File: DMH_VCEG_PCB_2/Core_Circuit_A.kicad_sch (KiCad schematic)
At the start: 78 parts, among them J22 Conn_01x10_PinHeader, Q1 BC548, Q2 BC558, Q3 BC548, SW1 SW_DPDT_x2, U1 TL074, U2 4001, U3 40106, U4 CD4066BE, U5 TL074, U6 TL074, U7 TL074

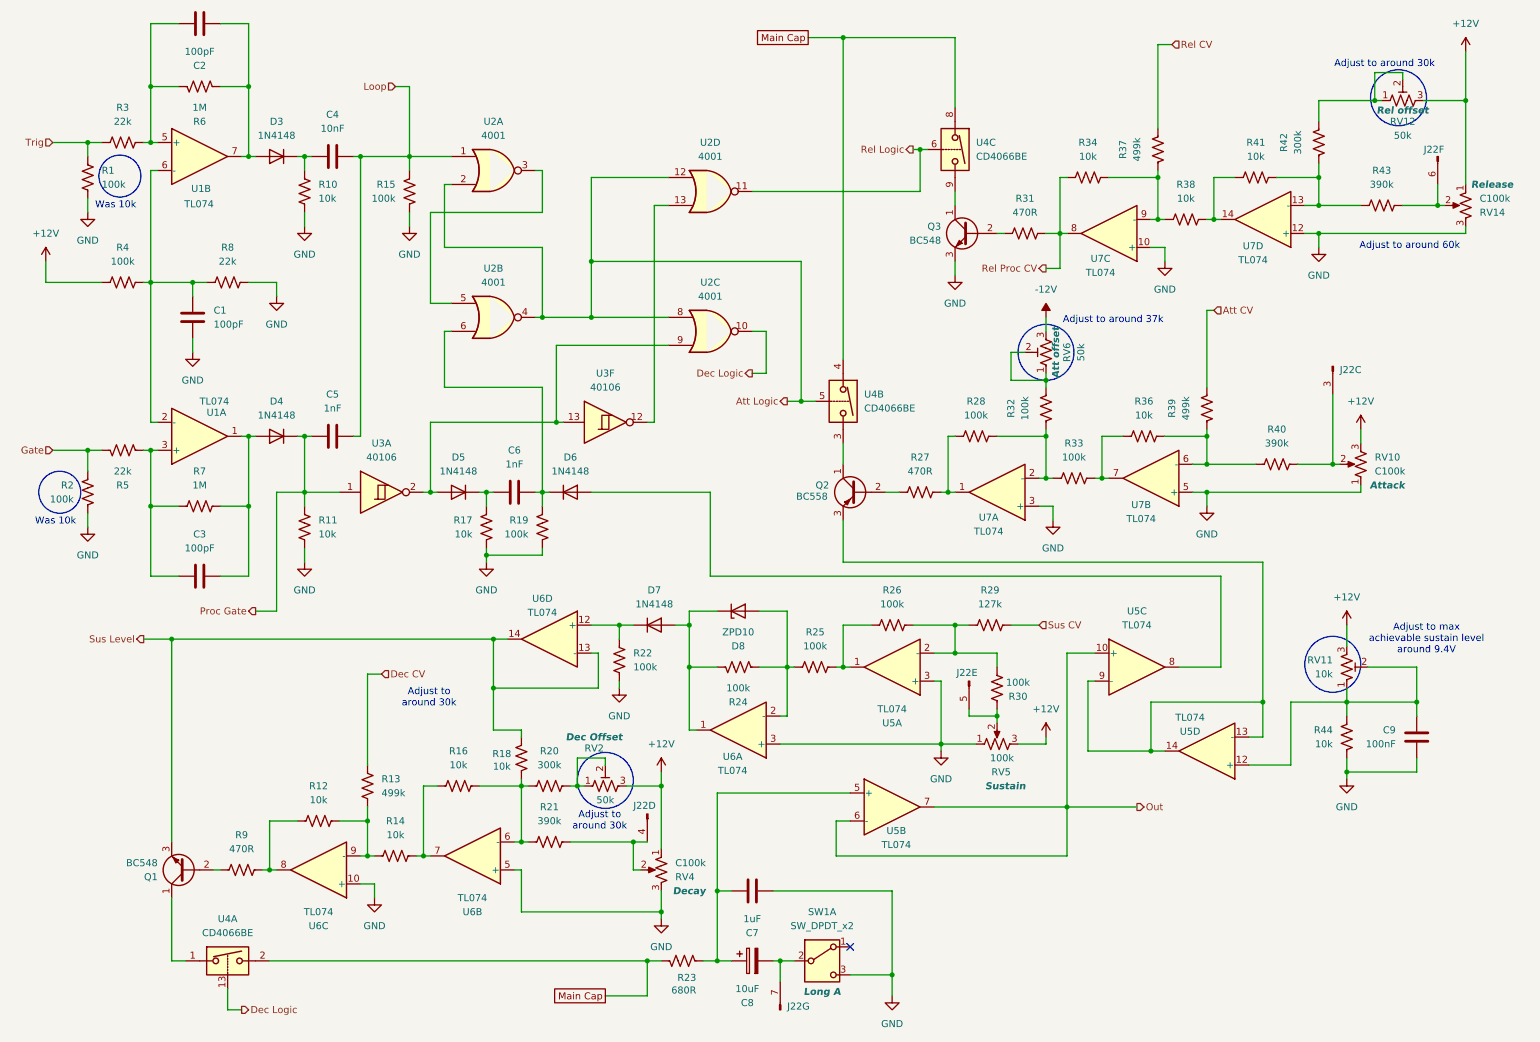
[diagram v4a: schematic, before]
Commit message: Synced PCB 2 project with PCB 1
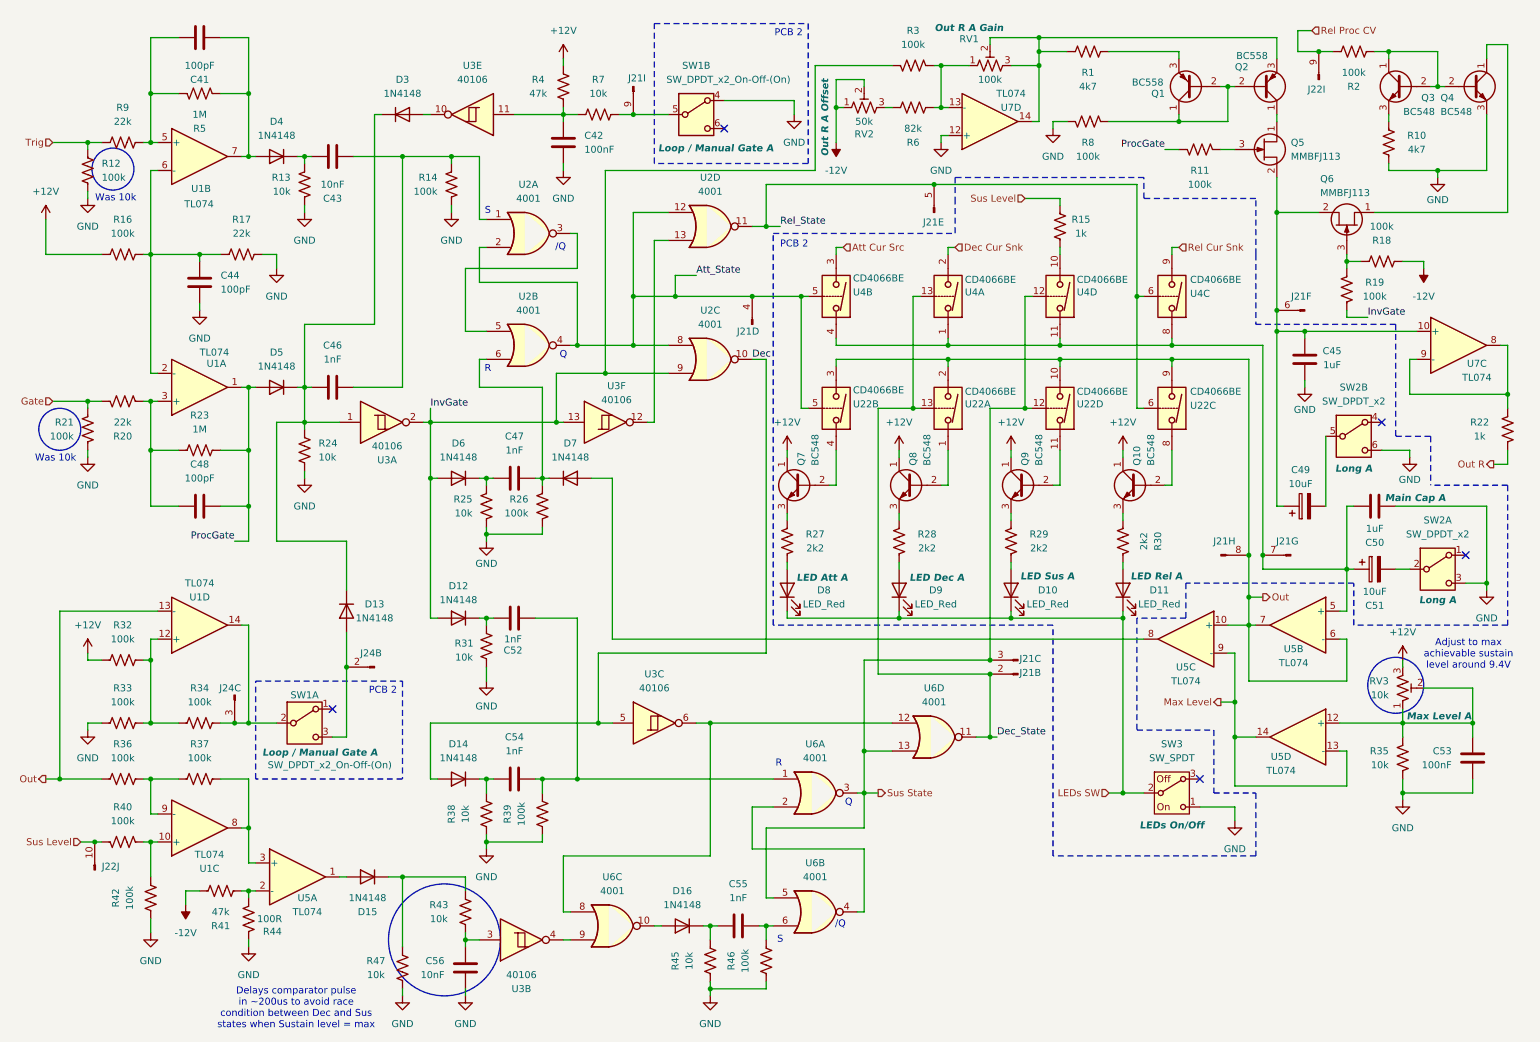
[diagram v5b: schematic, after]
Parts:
- removed D7: 1N4148, Diode_THT:D_DO-35_SOD27_P7.62mm_Horizontal, symbol Diode:1N4148
- removed D8: ZPD10, Diode_THT:D_DO-35_SOD27_P7.62mm_Horizontal, symbol Diode:ZPDxx
- removed J22: Conn_01x10_PinHeader, Connector_PinSocket_2.54mm:PinSocket_1x10_P2.54mm_Vertical, symbol SynthStuff:Conn_01x10_PinHeader
- removed Q1: BC548, Package_TO_SOT_THT:TO-92L_Inline_Wide, symbol Transistor_BJT:BC548
- removed R12, R14, R16: 10k, Resistor_THT:R_Axial_DIN0207_L6.3mm_D2.5mm_P7.62mm_Horizontal, symbol Device:R_US
- removed R13: 499k, Resistor_THT:R_Axial_DIN0207_L6.3mm_D2.5mm_P7.62mm_Horizontal, symbol Device:R_US
- removed R20: 300k, Resistor_THT:R_Axial_DIN0207_L6.3mm_D2.5mm_P7.62mm_Horizontal, symbol Device:R_US
- removed R21: 390k, Resistor_THT:R_Axial_DIN0207_L6.3mm_D2.5mm_P7.62mm_Horizontal, symbol Device:R_US
- removed R23: 680R, Resistor_THT:R_Axial_DIN0207_L6.3mm_D2.5mm_P7.62mm_Horizontal, symbol Device:R_US
- removed R24, R25, R26: 100k, Resistor_THT:R_Axial_DIN0207_L6.3mm_D2.5mm_P7.62mm_Horizontal, symbol Device:R_US
- removed R9: 470R, Resistor_THT:R_Axial_DIN0207_L6.3mm_D2.5mm_P7.62mm_Horizontal, symbol Device:R_US
- removed RV10, RV14, RV4: C100k, SynthStuff:Potentiometer_Alpha_RD901F-40-00D_Single_Vertical, symbol Device:R_Potentiometer_US
- removed RV12, RV6: 50k, Potentiometer_THT:Potentiometer_Bourns_3296W_Vertical, symbol Device:R_Potentiometer_Trim_US
- removed RV5: 100k, SynthStuff:Potentiometer_Alpha_RD901F-40-00D_Single_Vertical, symbol Device:R_Potentiometer_US
- removed U6: TL074, Package_DIP:DIP-14_W7.62mm_Socket, symbol Amplifier_Operational:TL074
- removed unit 2 of U7
- removed unit 1 of U7
- added C42: 100nF, Capacitor_THT:C_Disc_D4.3mm_W1.9mm_P5.00mm, symbol Device:C
- added C45: 1uF, Capacitor_THT:C_Rect_L7.0mm_W4.5mm_P5.00mm, symbol Device:C
- added C49: 10uF, Capacitor_THT:CP_Radial_D4.0mm_P1.50mm, symbol Device:C_Polarized
- added C52, C54, C55: 1nF, Capacitor_THT:C_Disc_D4.3mm_W1.9mm_P5.00mm, symbol Device:C
- added C56: 10nF, Capacitor_THT:C_Disc_D4.3mm_W1.9mm_P5.00mm, symbol Device:C
- added D10, D11, D8, D9: LED_Red, LED_THT:LED_D3.0mm, symbol Device:LED
- added D12, D13, D14, D15, D16, D3: 1N4148, Diode_THT:D_DO-35_SOD27_P7.62mm_Horizontal, symbol Diode:1N4148
- added J21: Conn_01x10_PinHeader, Connector_PinHeader_2.54mm:PinHeader_1x10_P2.54mm_Vertical, symbol SynthStuff:Conn_01x10_PinHeader
- added J22: Conn_01x10_PinHeader, Connector_PinSocket_2.54mm:PinSocket_1x10_P2.54mm_Vertical, symbol SynthStuff:Conn_01x10_PinHeader
- added J24: Conn_01x06_PinHeader, Connector_PinHeader_2.54mm:PinHeader_1x06_P2.54mm_Vertical, symbol SynthStuff:Conn_01x06_PinHeader
- added Q1: BC558, Package_TO_SOT_THT:TO-92L_Inline_Wide, symbol Transistor_BJT:BC558
- added Q10, Q4, Q7, Q8, Q9: BC548, Package_TO_SOT_THT:TO-92L_Inline_Wide, symbol Transistor_BJT:BC548
- added Q5, Q6: MMBFJ113, Package_TO_SOT_THT:TO-92L_Inline, symbol Transistor_FET:MMBFJ113
- added R1, R10: 4k7, Resistor_THT:R_Axial_DIN0207_L6.3mm_D2.5mm_P7.62mm_Horizontal, symbol Device:R_US
- added R11, R19, R2, R3, R46, R8: 100k, Resistor_THT:R_Axial_DIN0207_L6.3mm_D2.5mm_P7.62mm_Horizontal, symbol Device:R_US
- added R15: 1k, Resistor_THT:R_Axial_DIN0207_L6.3mm_D2.5mm_P7.62mm_Horizontal, symbol Device:R_US
- added R4: 47k, Resistor_THT:R_Axial_DIN0207_L6.3mm_D2.5mm_P7.62mm_Horizontal, symbol Device:R_US
- added R44: 100R, Resistor_THT:R_Axial_DIN0207_L6.3mm_D2.5mm_P7.62mm_Horizontal, symbol Device:R_US
- added R45, R47, R7: 10k, Resistor_THT:R_Axial_DIN0207_L6.3mm_D2.5mm_P7.62mm_Horizontal, symbol Device:R_US
- added R6: 82k, Resistor_THT:R_Axial_DIN0207_L6.3mm_D2.5mm_P7.62mm_Horizontal, symbol Device:R_US
- added RV1: 100k, Potentiometer_THT:Potentiometer_Bourns_3296W_Vertical, symbol Device:R_Potentiometer_Trim_US
- added SW1: SW_DPDT_x2_On-Off-(On), SynthStuff:Toggle_Switch_2_Poles_TE, symbol Switch:SW_DPDT_x2
- added unit 2 of SW2
- added SW3: SW_SPDT, SynthStuff:Toggle_Switch_TE, symbol SynthStuff:SW_SPDT_321_OnOff
- added unit 3 of U1
- added unit 4 of U1
- added U22: CD4066BE, Package_DIP:DIP-14_W7.62mm, symbol Analog_Switch:CD4066BE
- added unit 3 of U3
- added unit 2 of U3
- added unit 5 of U3
- added unit 4 of U4
- added U6: 4001, Package_DIP:DIP-14_W7.62mm_Socket, symbol 4xxx:4001
- C50: renamed from C7; footprint Capacitor_THT:C_Disc_D4.3mm_W1.9mm_P5.00mm -> Capacitor_THT:C_Rect_L7.0mm_W4.5mm_P5.00mm; Function (none) -> Main Cap A
- C51: renamed from C8; footprint Capacitor_THT:CP_Radial_D5.0mm_P2.00mm -> Capacitor_THT:CP_Radial_D4.0mm_P1.50mm
- R18, R34, R36: value 10k -> 100k
- R22: value 100k -> 1k
- R27: value 470R -> 2k2
- R28, R30: value 100k -> 2k2
- R29: value 127k -> 2k2
- R31: value 470R -> 10k
- R37, R39: value 499k -> 100k
- R40: value 390k -> 100k
- R41: value 10k -> 47k
- R42: value 300k -> 100k
- R43: value 390k -> 10k
- RV2: Function Dec Offset -> Out R A Offset
- RV3: renamed from RV11; Function (none) -> Max Level A
- renumbered C2 to C41, C4 to C43, C1 to C44, C5 to C46, C6 to C47, C3 to C48, C9 to C53, D3 to D4, D4 to D5, D5 to D6, D6 to D7, R1 to R12, R10 to R13, R15 to R14, R4 to R16, R8 to R17, R5 to R20, R2 to R21, R7 to R23, R11 to R24, R17 to R25, R19 to R26, R44 to R35, R6 to R5, R3 to R9, SW1 to SW2
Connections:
- net Att CV is gone; now on net GND: R39.2
- net +12V: now also R32.2, Q10.1 (C), Q7.1 (C), Q8.1 (C), Q9.1 (C), R4.1; no longer RV2.3
- net -12V: now also R18.1, R41.1, RV2.1, RV2.2
- net GND: now also R31.2, R33.2, R38.2, R42.2, C42.2, C45.1, C56.1, Q4.3 (E), R10.1, R44.2, R45.2, R46.2, R47.2, R8.2, SW1.4 (A), SW2.6 (C), SW3.1 (C); no longer Q3.3 (E), R22.1, U5.3 (+), U7.10 (+)
- net Out: now also R36.2, J21.8 (Pin_8), U1.13 (-), U22.10, U22.2, U22.3, U22.9
- net Rel Proc CV: now also J22.9 (Pin_9), R2.1; no longer R31.1, R34.2, U7.8
- net Sus Level: now also R40.1, J22.10 (Pin_10), R15.2; no longer R18.2
- net Max Level: now reaches U5.13 (-), U5.14, U5.9 (-)
- net Max Level: no longer Q2.3 (E)
- net at R22.2: now also U7.8, U7.9 (-)
- net at U5.1: now also D15.2 (A)
- net at R33.1: now also R32.1, R34.2, U1.12 (+); no longer R36.2
- net at C50.1, C51.1, U5.5 (+): now also U4.1, U4.4, U4.8, J21.7 (Pin_7), U4.11
- net at R43.1: now also D15.1 (K), R47.1
- net InvGate: now reaches D6.2 (A), U2.9, U3.13, U3.2
- net InvGate: now also D12.2 (A), R19.2, R3.1
- net at Q3.1 (C): now also Q3.2 (B), Q4.2 (B), R2.2; no longer U4.9
- net ProcGate: now reaches C48.2, D5.2 (A), R23.1, U1.1
- net ProcGate: now also R11.2
- net at Q2.1 (C): now also Q5.1 (D); no longer U4.3
- net at R27.2: now also D8.2 (A); no longer Q2.2 (B)
- net at R28.2: now also D9.2 (A); no longer R27.1
- net at R30.1: now also Q10.3 (E)
- net Att Logic renamed Att_State
- net Att_State: now also J21.4 (Pin_4), U22.5
- net Dec Logic renamed Dec
- net Dec: now also D14.2 (A), U3.5; no longer U4.13
- net Loop: no longer names the net of C43.2, C46.2, R14.2, U2.1
- removed net Main Cap: U4.2, U4.4, U4.8
- net Proc Gate: no longer names the net of C46.1, D5.1 (K), R24.2, U3.1
- net Proc Gate: now also D13.1 (K), D3.1 (K)
- net Rel CV: no longer names the net of R37.2
- net Rel CV: now also R36.1, U1.9 (-)
- net Rel Logic renamed Rel_State
- net Rel_State: now also J21.5 (Pin_5), U22.6
- net Sus CV: no longer names the net of R29.1
- net Sus CV: now also Q9.3 (E)
- new net: Q9.2 (B), U22.11
- new net: Q6.3 (G), R18.2, R19.1
- new net: C52.2, C54.2, R39.1, U6.1
- new net: C56.2, R43.2, U3.3
- new net: C45.2, C49.1, J21.6 (Pin_6), Q5.2 (S), Q6.2 (S), U7.10 (+)
- new net: J21.9 (Pin_9), R7.1, SW1.5 (B)
- new net: C42.1, R4.2, R7.2, U3.11
- new net: D16.2 (A), U6.10
- new net: U3.6, U6.12, U6.8
- new net: U3.4, U6.9
- new net: U6.2, U6.4
- new net: C55.2, R46.1, U6.6
- new net: C54.1, D14.1 (K), R38.1
- new net: Q5.3 (G), R11.1
- new net: R40.2, R42.1, U1.10 (+)
- new net: R37.1, U1.8, U5.3 (+)
- new net: R6.1, RV2.3
- new net: R3.2, R6.2, RV1.1, U7.13 (-)
- new net: Q10.2 (B), U22.8
- new net: Q7.3 (E), R27.1
- new net: Q2.3 (E), R1.1, RV1.2, RV1.3, U7.14
- new net: Q4.1 (C), Q6.1 (D)
- new net: Q1.1 (C), Q1.2 (B), Q2.2 (B), R8.1
- new net: Q1.3 (E), R1.2
- new net: D11.2 (A), R30.2
- new net: Q8.2 (B), U22.1
- new net: D3.2 (A), U3.10
- new net: C55.1, D16.1 (K), R45.1
- new net: C52.1, D12.1 (K), R31.1
- new net: Q7.2 (B), U22.4
- new net: R15.1, U4.10
- new net: R41.2, R44.1, U5.2 (-)
- new net: J24.3 (Pin_3), R34.1, SW1.2 (B), U1.14
- new net: D13.2 (A), J24.2 (Pin_2), SW1.3 (C)
- new net: Q8.3 (E), R28.1
- new net: C49.2, SW2.5 (B)
- new net: D10.2 (A), R29.2
- new net: Q3.3 (E), R10.2
- new net Att Cur Src: U4.3
- new net Dec Cur Snk: U4.2
- new net Dec_State: J21.2 (Pin_2), U22.13, U4.13, U6.11
- new net LEDs SW: D10.1 (K), D11.1 (K), D8.1 (K), D9.1 (K), SW3.2 (B)
- new net Out R: R22.1
- new net Rel Cur Snk: U4.9
- new net Sus State: J21.3 (Pin_3), U22.12, U4.12, U6.13, U6.3, U6.5
- no-connect marks 1 -> 5
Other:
- note added: "/Q"
- note added: "Delays comparator pulse in ~200us to avoid race condition between Dec and Sus states when Sustain level = max"
- note added: "PCB 2"
- note added: "Q"
- note added: "R"
- note added: "S"
- note removed: "Adjust to around 30k"
- note removed: "Adjust to around 37k"
- note removed: "Adjust to around 60k"
- moved on the sheet: C41, C44, C46, C47, C48, C50, C51, C53, D5, D6, D7, R12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

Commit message: Started placement on PCB 2
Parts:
- J21: footprint Connector_PinHeader_2.54mm:PinHeader_1x10_P2.54mm_Vertical -> Connector_PinSocket_2.54mm:PinSocket_1x10_P2.54mm_Vertical
- J24: footprint Connector_PinHeader_2.54mm:PinHeader_1x06_P2.54mm_Vertical -> Connector_PinSocket_2.54mm:PinSocket_1x06_P2.54mm_Vertical
- U22, U4: footprint Package_DIP:DIP-14_W7.62mm -> Package_DIP:DIP-14_W7.62mm_Socket
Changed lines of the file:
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@@
 			)
 		)
-		(property "Footprint" "Connector_PinHeader_2.54mm:PinHeader_1x10_P2.54mm_Vertical"
+		(property "Footprint" "Connector_PinSocket_2.54mm:PinSocket_1x10_P2.54mm_Vertical"
 			(at 243.84 110.49 0)
 			(effects
@@
 			)
 		)
-		(property "Footprint" "Connector_PinHeader_2.54mm:PinHeader_1x10_P2.54mm_Vertical"
+		(property "Footprint" "Connector_PinSocket_2.54mm:PinSocket_1x10_P2.54mm_Vertical"
 			(at 194.31 132.08 0)
 			(effects
@@
 			)
 		)
-		(property "Footprint" "Connector_PinHeader_2.54mm:PinHeader_1x10_P2.54mm_Vertical"
+		(property "Footprint" "Connector_PinSocket_2.54mm:PinSocket_1x10_P2.54mm_Vertical"
 			(at 179.07 48.26 0)
 			(effects
@@
 			)
 		)
-		(property "Footprint" "Connector_PinHeader_2.54mm:PinHeader_1x10_P2.54mm_Vertical"
+		(property "Footprint" "Connector_PinSocket_2.54mm:PinSocket_1x10_P2.54mm_Vertical"
 			(at 124.46 25.4 0)
 			(effects
@@
 			)
 		)
-		(property "Footprint" "Package_DIP:DIP-14_W7.62mm"
+		(property "Footprint" "Package_DIP:DIP-14_W7.62mm_Socket"
 			(at 179.07 83.82 0)
 			(effects
@@
 			)
 		)
-		(property "Footprint" "Package_DIP:DIP-14_W7.62mm"
+		(property "Footprint" "Package_DIP:DIP-14_W7.62mm_Socket"
 			(at 158.75 83.82 0)
 			(effects
@@
 			)
 		)
-		(property "Footprint" "Package_DIP:DIP-14_W7.62mm"
+		(property "Footprint" "Package_DIP:DIP-14_W7.62mm_Socket"
 			(at 199.39 63.5 0)
 			(effects
@@
 			)
 		)
-		(property "Footprint" "Connector_PinHeader_2.54mm:PinHeader_1x06_P2.54mm_Vertical"
+		(property "Footprint" "Connector_PinSocket_2.54mm:PinSocket_1x06_P2.54mm_Vertical"
 			(at 77.47 130.81 0)
 			(effects
@@
 			)
 		)
-		(property "Footprint" "Package_DIP:DIP-14_W7.62mm"
+		(property "Footprint" "Package_DIP:DIP-14_W7.62mm_Socket"
 			(at 179.07 63.5 0)
 			(effects
@@
 			)
 		)
-		(property "Footprint" "Connector_PinHeader_2.54mm:PinHeader_1x10_P2.54mm_Vertical"
+		(property "Footprint" "Connector_PinSocket_2.54mm:PinSocket_1x10_P2.54mm_Vertical"
 			(at 231.14 110.49 0)
 			(effects
@@
 			)
 		)
-		(property "Footprint" "Package_DIP:DIP-14_W7.62mm"
+		(property "Footprint" "Package_DIP:DIP-14_W7.62mm_Socket"
 			(at 199.39 83.82 0)
 			(effects
@@
 			)
 		)
-		(property "Footprint" "Connector_PinHeader_2.54mm:PinHeader_1x10_P2.54mm_Vertical"
+		(property "Footprint" "Connector_PinSocket_2.54mm:PinSocket_1x10_P2.54mm_Vertical"
 			(at 194.31 129.54 0)
 			(effects
@@
 			)
 		)
-		(property "Footprint" "Connector_PinHeader_2.54mm:PinHeader_1x10_P2.54mm_Vertical"
+		(property "Footprint" "Connector_PinSocket_2.54mm:PinSocket_1x10_P2.54mm_Vertical"
 			(at 146.05 68.58 0)
 			(effects
@@
 			)
 		)
-		(property "Footprint" "Package_DIP:DIP-14_W7.62mm"
+		(property "Footprint" "Package_DIP:DIP-14_W7.62mm_Socket"
 			(at 219.71 63.5 0)
 			(effects
@@
 			)
 		)
-		(property "Footprint" "Package_DIP:DIP-14_W7.62mm"
+		(property "Footprint" "Package_DIP:DIP-14_W7.62mm_Socket"
 			(at 219.71 83.82 0)
 			(effects
@@
 			)
 		)
-		(property "Footprint" "Connector_PinHeader_2.54mm:PinHeader_1x10_P2.54mm_Vertical"
+		(property "Footprint" "Connector_PinSocket_2.54mm:PinSocket_1x10_P2.54mm_Vertical"
 			(at 246.38 66.04 0)
 			(effects
@@
 			)
 		)
-		(property "Footprint" "Package_DIP:DIP-14_W7.62mm"
+		(property "Footprint" "Package_DIP:DIP-14_W7.62mm_Socket"
 			(at 158.75 63.5 0)
 			(effects
@@
 			)
 		)
-		(property "Footprint" "Connector_PinHeader_2.54mm:PinHeader_1x06_P2.54mm_Vertical"
+		(property "Footprint" "Connector_PinSocket_2.54mm:PinSocket_1x06_P2.54mm_Vertical"
 			(at 52.07 135.89 0)
 			(effects
